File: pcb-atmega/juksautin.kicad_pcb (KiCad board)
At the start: 2 copper layers, 65 x 35 mm, 27 parts, among them J1 Screw_Terminal_01x09, J3 AVR-ISP-6, J4 Conn_01x09, U1 SP3485EN, U2 SRV05-4, U3 R-78E5.0-0.5, U4 ATmega328P-AU, Y1 X322516MLB4SI

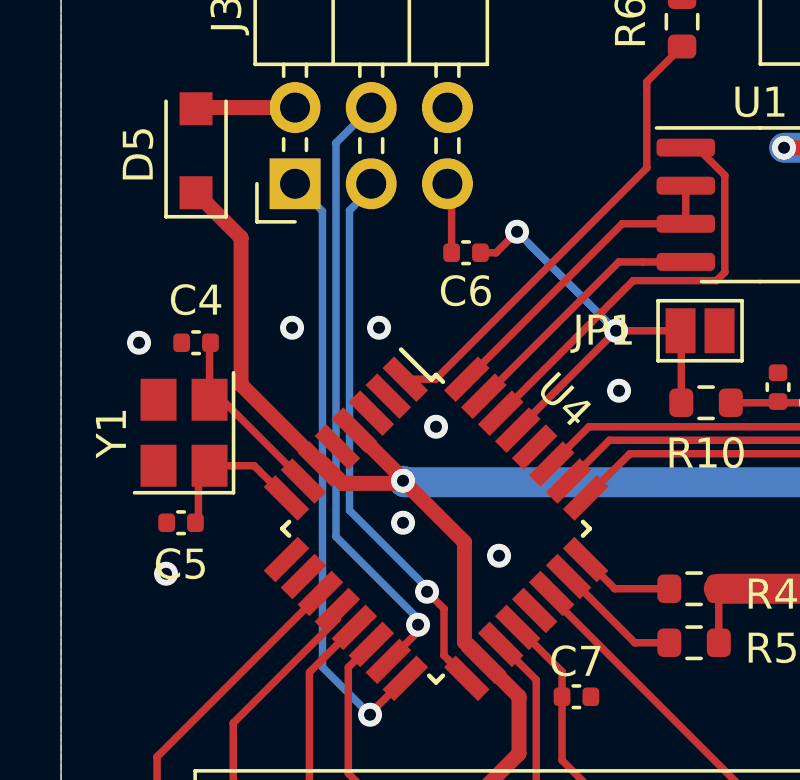
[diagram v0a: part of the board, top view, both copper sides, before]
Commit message: Schema and layout fixes after v0.9
- Crystal Y1 symbol changed to 4-pin, affecting the wiring as well
- Remove DC block capacitor C6, blocked RESET signal
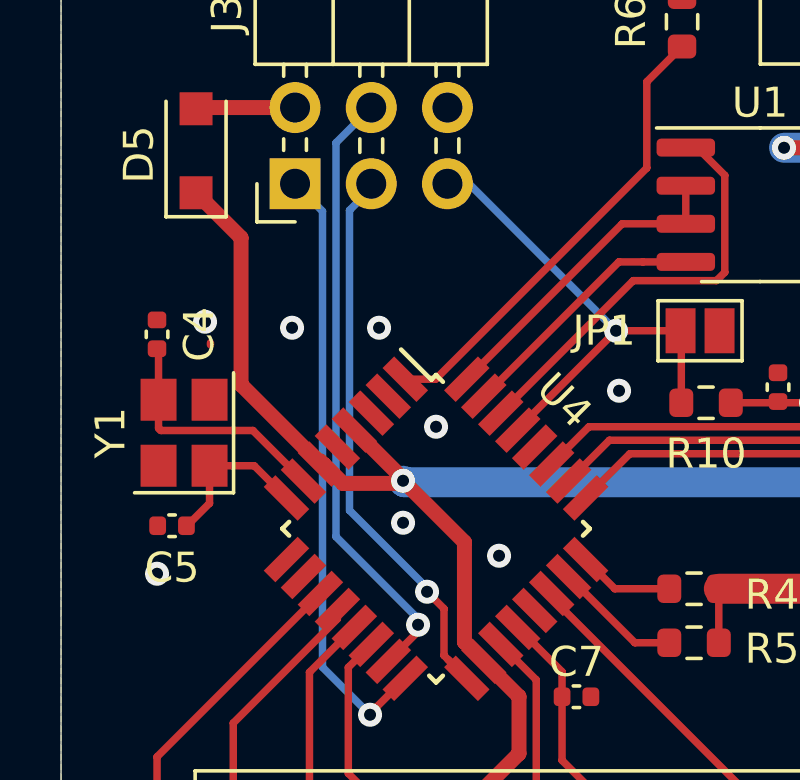
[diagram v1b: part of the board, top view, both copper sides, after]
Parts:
- removed C6: 100n, Capacitor_SMD:C_0402_1005Metric
- moved C4 1.33 mm to (113.2, 81.3), turned to 90 degrees
- moved C5 0.32 mm to (113.7, 87.7)
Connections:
- J3 pad 5: /RESET_IN -> /RESET
- Y1 pad 2: Net-(C4-Pad1) -> GND
- Y1 pad 3: (no net) -> Net-(C4-Pad1)
- Y1 pad 4: (no net) -> GND
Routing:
- net /RESET: track 19.6 -> 17.1 mm, vias 2 -> 1
- net /RESET_IN: track 2.30 -> 0.00 mm
- net Net-(C4-Pad1): track 6.17 -> 8.33 mm
